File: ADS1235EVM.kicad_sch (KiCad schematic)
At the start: 63 parts, among them J1 Conn_01x04_Pin, J2 Conn_01x06_Pin, J3 Conn_01x05_Pin, U1 ADS1235QWRHMRQ1, U2 LM27762, U5 UCC27524DGN

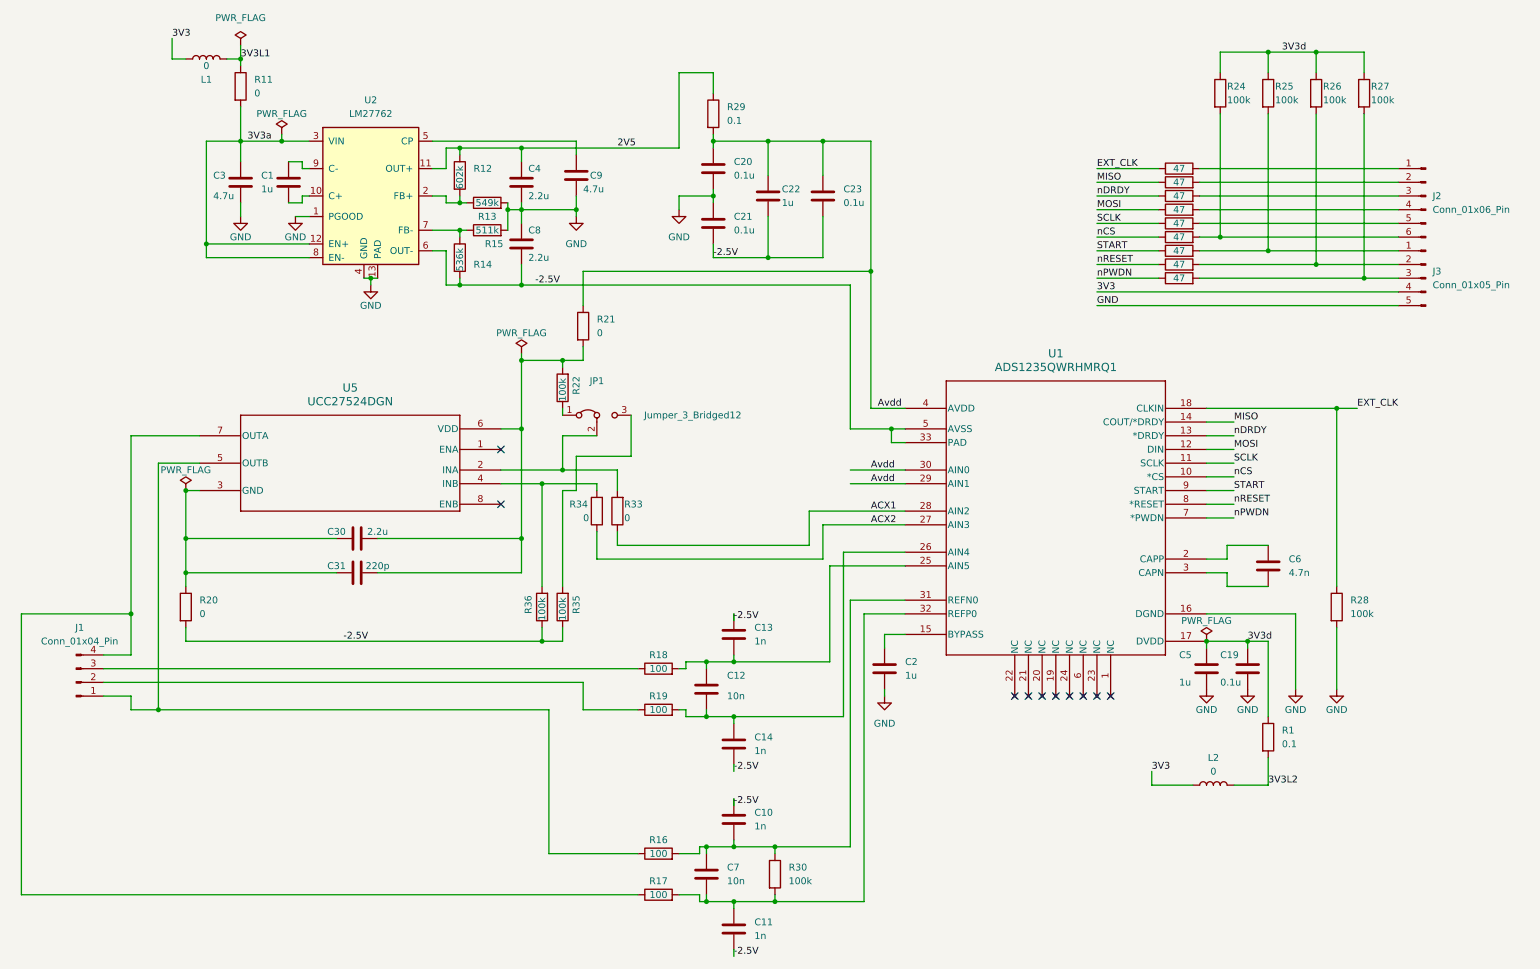
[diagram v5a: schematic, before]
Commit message: KiCAD - Add of load cell measurement
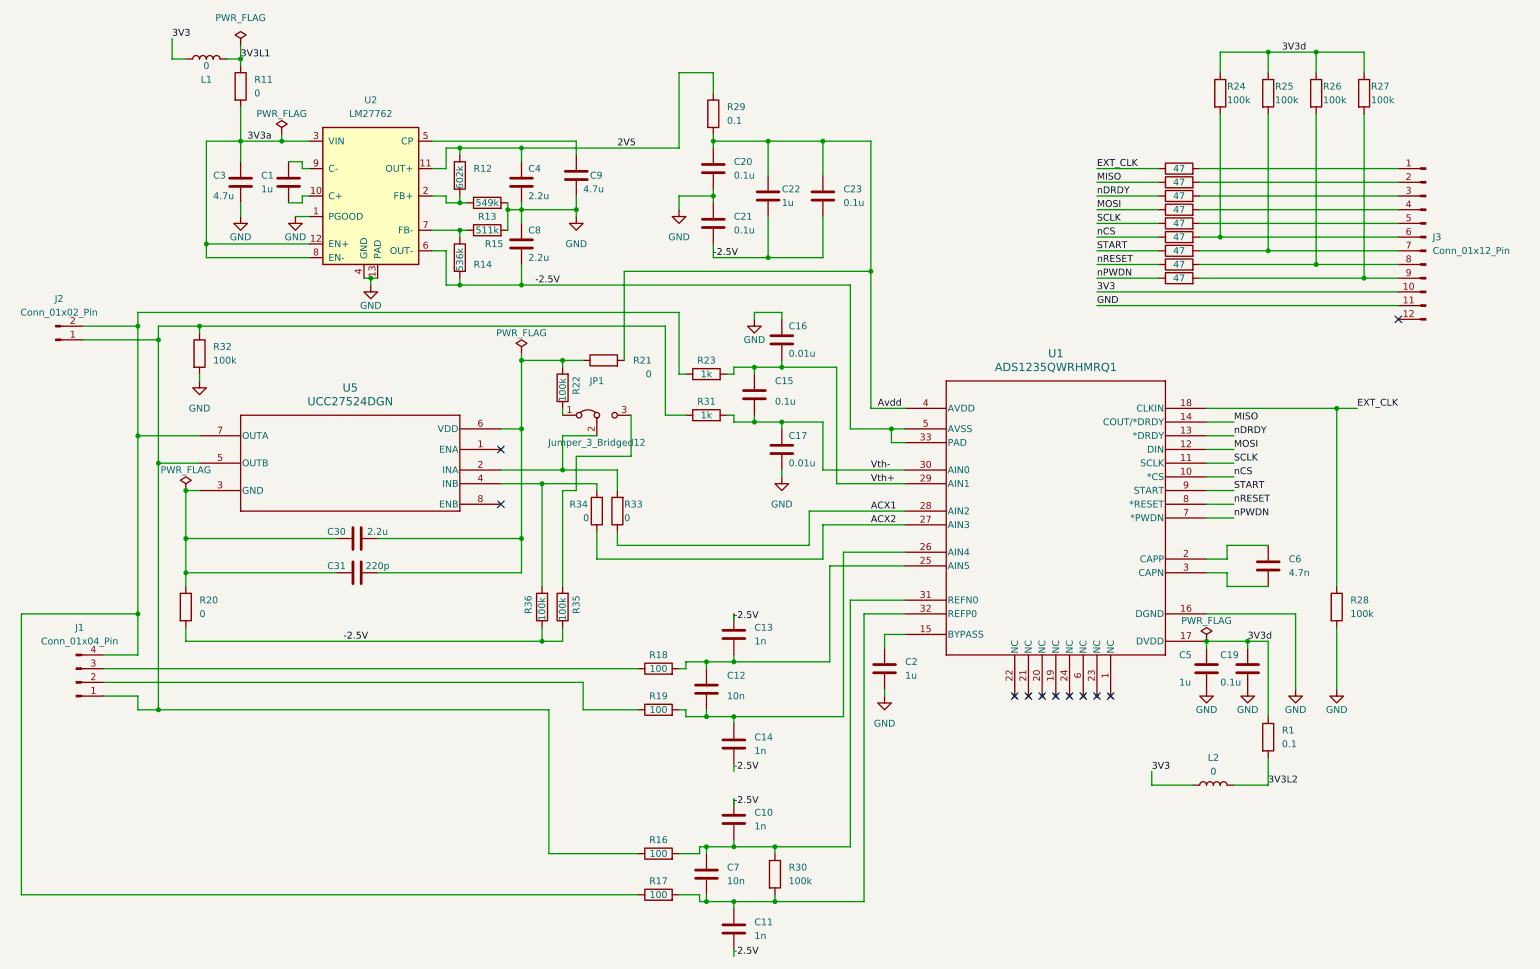
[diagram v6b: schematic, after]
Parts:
- removed J2: Conn_01x06_Pin, Connector_PinHeader_2.54mm:PinHeader_1x06_P2.54mm_Vertical, symbol Connector:Conn_01x06_Pin
- removed J3: Conn_01x05_Pin, Connector_PinHeader_2.54mm:PinHeader_1x05_P2.54mm_Vertical, symbol Connector:Conn_01x05_Pin
- added C15: 0.1u, Capacitor_SMD:C_0402_1005Metric, symbol Device:C
- added C16, C17: 0.01u, Capacitor_SMD:C_0402_1005Metric, symbol Device:C
- added J2: Conn_01x02_Pin, Connector_Hirose:Hirose_DF13-02P-1.25DSA_1x02_P1.25mm_Vertical, symbol Connector:Conn_01x02_Pin
- added J3: Conn_01x12_Pin, Connector_PinHeader_2.54mm:PinHeader_2x06_P2.54mm_Vertical, symbol Connector:Conn_01x12_Pin
- added R23, R31: 1k, Resistor_SMD:R_0402_1005Metric, symbol Device:R
- added R32: 100k, Resistor_SMD:R_0402_1005Metric, symbol Device:R
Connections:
- net 3V3: now also J3.10 (Pin_10)
- net Avdd: now also R21.2; no longer R21.1, U1.29 (AIN1), U1.30 (AIN0)
- net GND: now also C16.1, C17.2, J3.11 (Pin_11), R32.2
- net at R26.2, R8.2: now also J3.8 (Pin_8)
- net at R7.2: now also J3.1 (Pin_1)
- net at R3.2: now also J3.2 (Pin_2)
- net at R2.2: now also J3.3 (Pin_3)
- net at R4.2: now also J3.4 (Pin_4)
- net at R5.2: now also J3.5 (Pin_5)
- net at R24.2, R6.2: now also J3.6 (Pin_6)
- net at J1.1 (Pin_1), R16.1, U5.5 (OUTB): now also J2.1 (Pin_1), R31.1, R32.1
- net at C30.2, C31.2, R22.2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: now also R21.1; no longer R21.2
- net at J1.4 (Pin_4), R17.1, U5.7 (OUTA): now also J2.2 (Pin_2), R23.1
- net at R10.2, R27.2: now also J3.9 (Pin_9)
- net at R25.2, R9.2: now also J3.7 (Pin_7)
- new net Vth+: C15.1, C16.2, R23.2, U1.29 (AIN1)
- new net Vth-: C15.2, C17.1, R31.2, U1.30 (AIN0)
- no-connect marks 10 -> 11
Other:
- moved on the sheet: R21
